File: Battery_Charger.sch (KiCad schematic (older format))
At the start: 48 parts, among them J8 USB_B_Micro, Q10 BC817, Q11 BC807, Q12 BSS138, Q13 BSS138, Q14 BSS138, Q9 BSS84, SW2 set_current, SW3 PWRON, U23 BQ24079RGT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

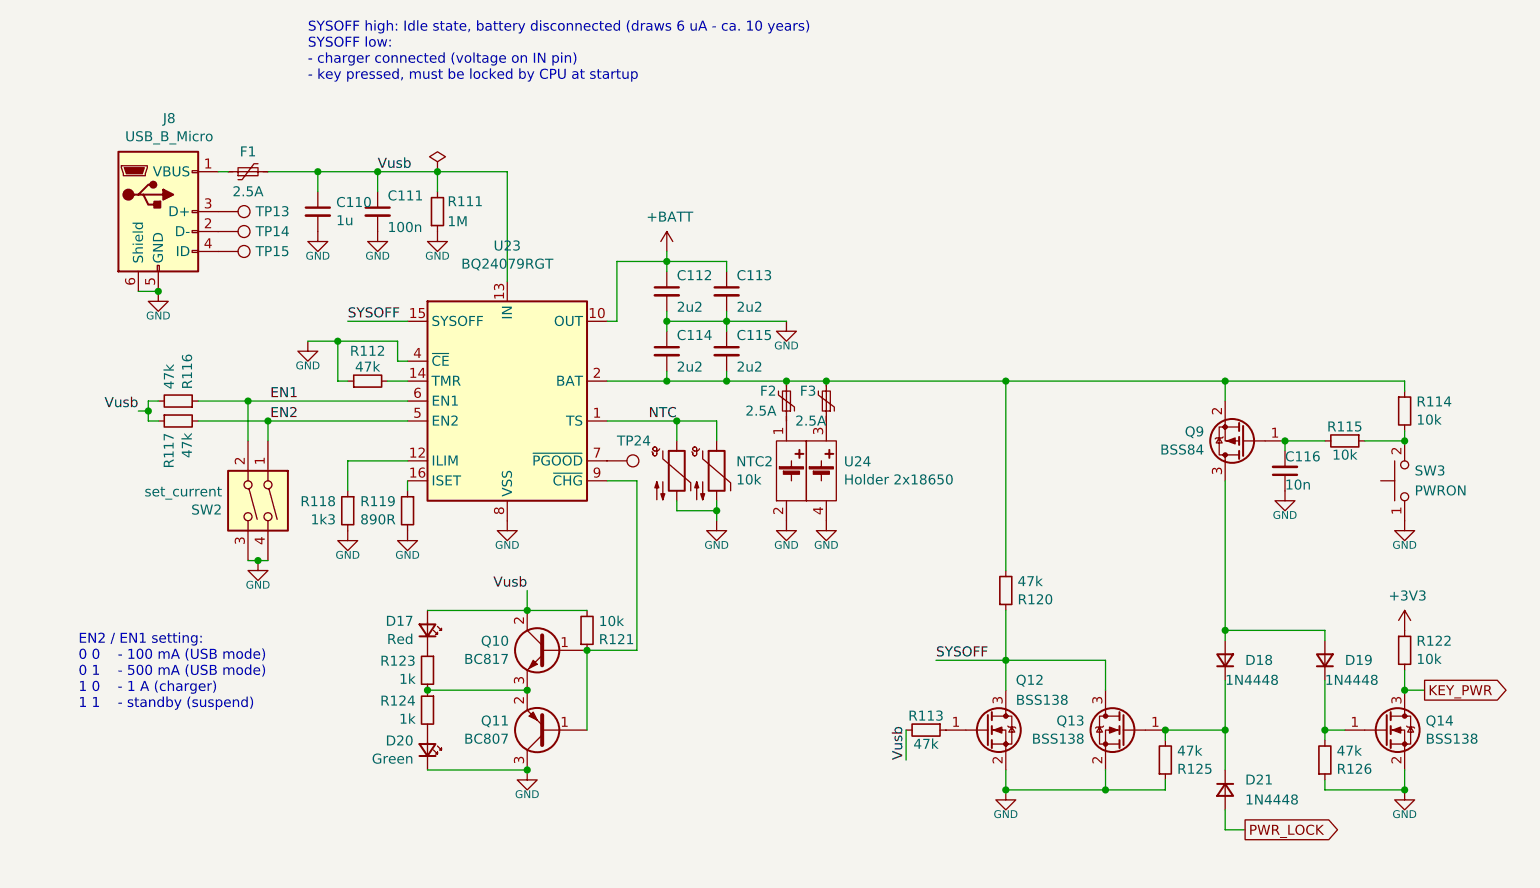
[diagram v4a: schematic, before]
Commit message: - as-built changes - add custom library elements
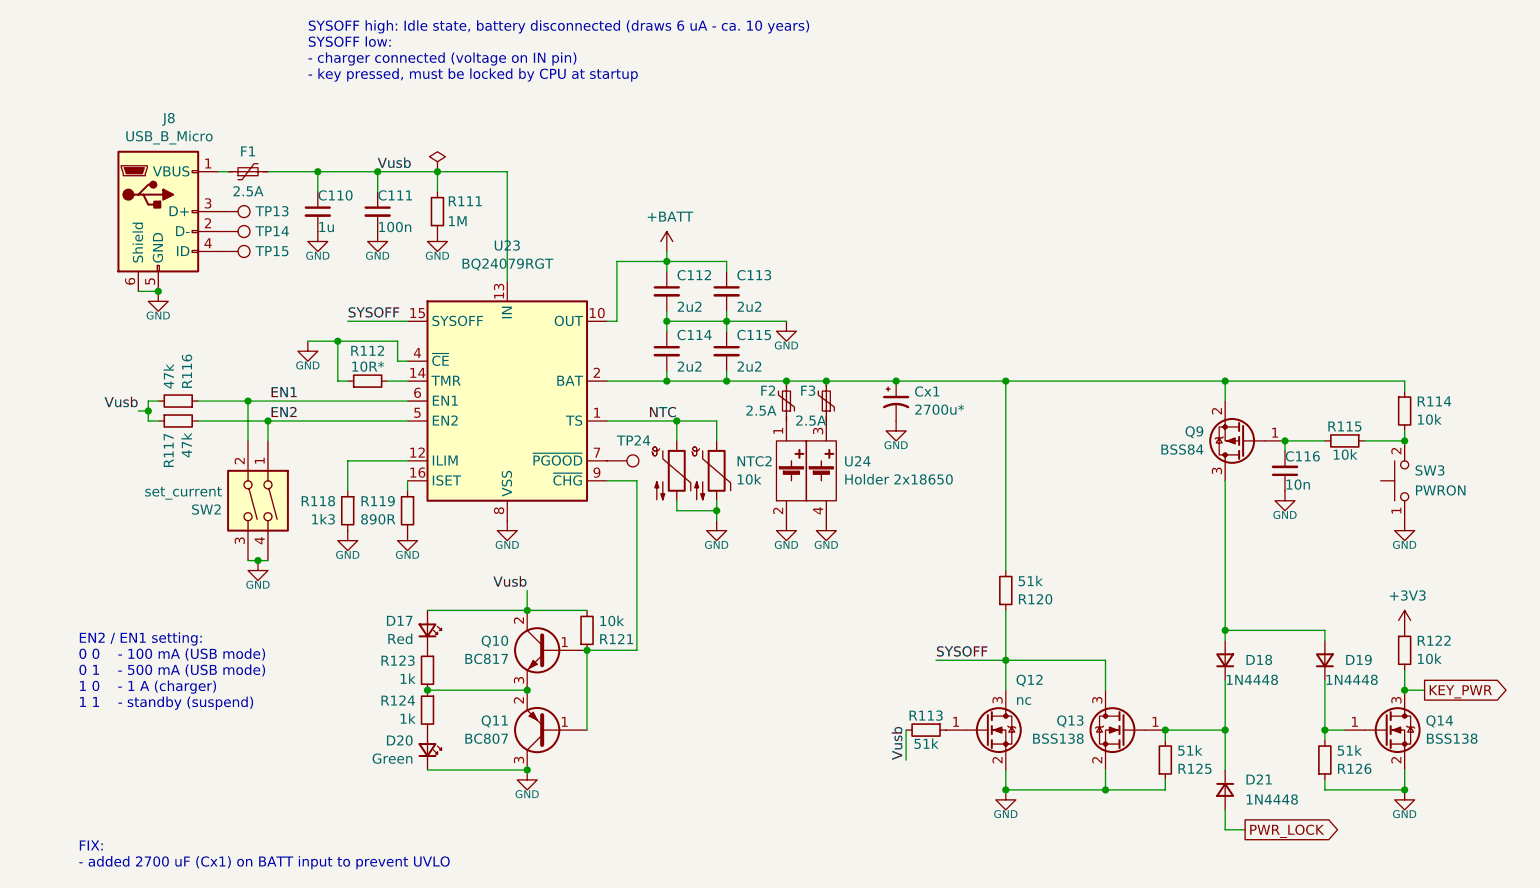
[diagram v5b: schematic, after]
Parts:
- added Cx1: 2700u*, symbol Device:CP1_Small
- Q12: value BSS138 -> nc
- R112: value 47k -> 10R*
- R113, R120, R125, R126: value 47k -> 51k
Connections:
- net GND: now also Cx1.2
- net at C114.2, C115.2, F2.2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: now also Cx1.1
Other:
- note added: "FIX:\n- added 2700 uF (Cx1) on BATT input to prevent UVLO"
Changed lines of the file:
@@
 $Descr A4 11693 8268
 encoding utf-8
-Sheet 7 10
-Title ""
-Date ""
-Rev ""
-Comp ""
+Sheet 6 10
+Title "Zasilanie - bateria"
+Date "2021-01-18"
+Rev "1.0"
+Comp "Łukasz Sitarek"
 Comment1 ""
 Comment2 ""
@@
 AR Path="/5F620813/5F7AA8D1" Ref="C?"  Part="1"
 AR Path="/5F7A93EE/5F7AA8D1" Ref="C110"  Part="1"
-F 0 "C110" H 3992 2496 50  0000 L CNN
-F 1 "1u" H 3992 2405 50  0000 L CNN
+F 0 "C110" H 3900 2500 50  0000 L BNN
+F 1 "1u" H 3900 2400 50  0000 L TNN
 F 2 "Capacitor_SMD:C_0603_1608Metric" H 3900 2450 50  0001 C CNN
 F 3 "~" H 3900 2450 50  0001 C CNN
@@
 AR Path="/5F7A93EE/5F7AA9E6" Ref="R112"  Part="1"
 F 0 "R112" V 4300 3300 50  0000 C CNN
-F 1 "47k" V 4250 3300 50  0000 C BNN
+F 1 "10R*" V 4250 3300 50  0000 C BNN
 F 2 "Resistor_SMD:R_0603_1608Metric" H 4150 3300 50  0001 C CNN
 F 3 "~" H 4150 3300 50  0001 C CNN
@@
 AR Path="/5F7A93EE/5F7AA9F5" Ref="R120"  Part="1"
 F 0 "R120" H 7409 4396 50  0000 L CNN
-F 1 "47k" H 7409 4305 50  0000 L CNN
+F 1 "51k" H 7409 4305 50  0000 L CNN
 F 2 "Resistor_SMD:R_0603_1608Metric" H 7350 4350 50  0001 C CNN
 F 3 "~" H 7350 4350 50  0001 C CNN
@@
 P 7250 5050
 F 0 "Q12" H 7400 5300 50  0000 L CNN
-F 1 "BSS138" H 7400 5200 50  0000 L CNN
+F 1 "nc" H 7400 5200 50  0000 L CNN
 F 2 "Package_TO_SOT_SMD:SOT-23" H 7450 4975 50  0001 L CIN
 F 3 "https://www.onsemi.com/pub/Collateral/NDS7002A-D.PDF" H 7250 5050 50  0001 L CNN
@@
 AR Path="/5F620813/5FE2517E" Ref="C?"  Part="1"
 AR Path="/5F7A93EE/5FE2517E" Ref="C111"  Part="1"
-F 0 "C111" H 4250 2500 50  0000 L BNN
-F 1 "100n" H 4250 2400 50  0000 L TNN
+F 0 "C111" H 4200 2500 50  0000 L BNN
+F 1 "100n" H 4200 2400 50  0000 L TNN
 F 2 "Capacitor_SMD:C_0603_1608Metric" H 4200 2450 50  0001 C CNN
 F 3 "~" H 4200 2450 50  0001 C CNN
@@
 AR Path="/5F7A93EE/5FE2CE43" Ref="R125"  Part="1"
 F 0 "R125" H 8209 5246 50  0000 L CNN
-F 1 "47k" H 8209 5155 50  0000 L CNN
+F 1 "51k" H 8209 5155 50  0000 L CNN
 F 2 "Resistor_SMD:R_0603_1608Metric" H 8150 5200 50  0001 C CNN
 F 3 "~" H 8150 5200 50  0001 C CNN
@@
 AR Path="/5F7A93EE/5FF5276E" Ref="R126"  Part="1"
 F 0 "R126" H 9009 5246 50  0000 L CNN
-F 1 "47k" H 9009 5155 50  0000 L CNN
+F 1 "51k" H 9009 5155 50  0000 L CNN
 F 2 "Resistor_SMD:R_0603_1608Metric" H 8950 5200 50  0001 C CNN
 F 3 "~" H 8950 5200 50  0001 C CNN
@@
 Connection ~ 8450 4550
 Wire Wire Line
-	6450 3300 7350 3300
+	6450 3300 6800 3300
 Wire Wire Line
 	8550 5550 8450 5550
@@
 AR Path="/5F7A93EE/5FB20FEF" Ref="R113"  Part="1"
 F 0 "R113" V 6850 5050 50  0000 C TNN
-F 1 "47k" V 7050 5050 50  0000 C BNN
+F 1 "51k" V 7050 5050 50  0000 C BNN
 F 2 "Resistor_SMD:R_0603_1608Metric" H 6950 5050 50  0001 C CNN
 F 3 "~" H 6950 5050 50  0001 C CNN
@@
 Text Label 5700 3500 2    50   ~ 0
 NTC
+$Comp
+L Device:CP1_Small C?
+U 1 1 5FE6743C
+P 6800 3400
+AR Path="/5F620813/5FE6743C" Ref="C?"  Part="1"
+AR Path="/5F7A93EE/5FE6743C" Ref="Cx1"  Part="1"
+F 0 "Cx1" H 6891 3446 50  0000 L CNN
+F 1 "2700u*" H 6891 3355 50  0000 L CNN
+F 2 "" H 6800 3400 50  0001 C CNN
+F 3 "~" H 6800 3400 50  0001 C CNN
+	1    6800 3400
+	1    0    0    -1
+$EndComp
+$Comp
+L power:GND #PWR?
+U 1 1 5FE6A5EB
+P 6800 3500
+AR Path="/5F40DCB9/5FE6A5EB" Ref="#PWR?"  Part="1"
+AR Path="/5F618AB9/5FE6A5EB" Ref="#PWR?"  Part="1"
+AR Path="/5FE6A5EB" Ref="#PWR?"  Part="1"
+AR Path="/5F620813/5FE6A5EB" Ref="#PWR?"  Part="1"
+AR Path="/5F7A93EE/5FE6A5EB" Ref="#PWR?"  Part="1"
+F 0 "#PWR?" H 6800 3340 50  0001 C CNN
+F 1 "GND" H 6800 3400 39  0000 C TNN
+F 2 "" H 6800 3500 50  0001 C CNN
+F 3 "" H 6800 3500 50  0001 C CNN
+	1    6800 3500
+	1    0    0    -1
+$EndComp
+Connection ~ 6800 3300
+Wire Wire Line
+	6800 3300 7350 3300
+Text Notes 2700 5750 0    50   ~ 0
+FIX:\n- added 2700 uF (Cx1) on BATT input to prevent UVLO
 $EndSCHEMATC
